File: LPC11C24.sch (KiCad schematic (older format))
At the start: 1 part

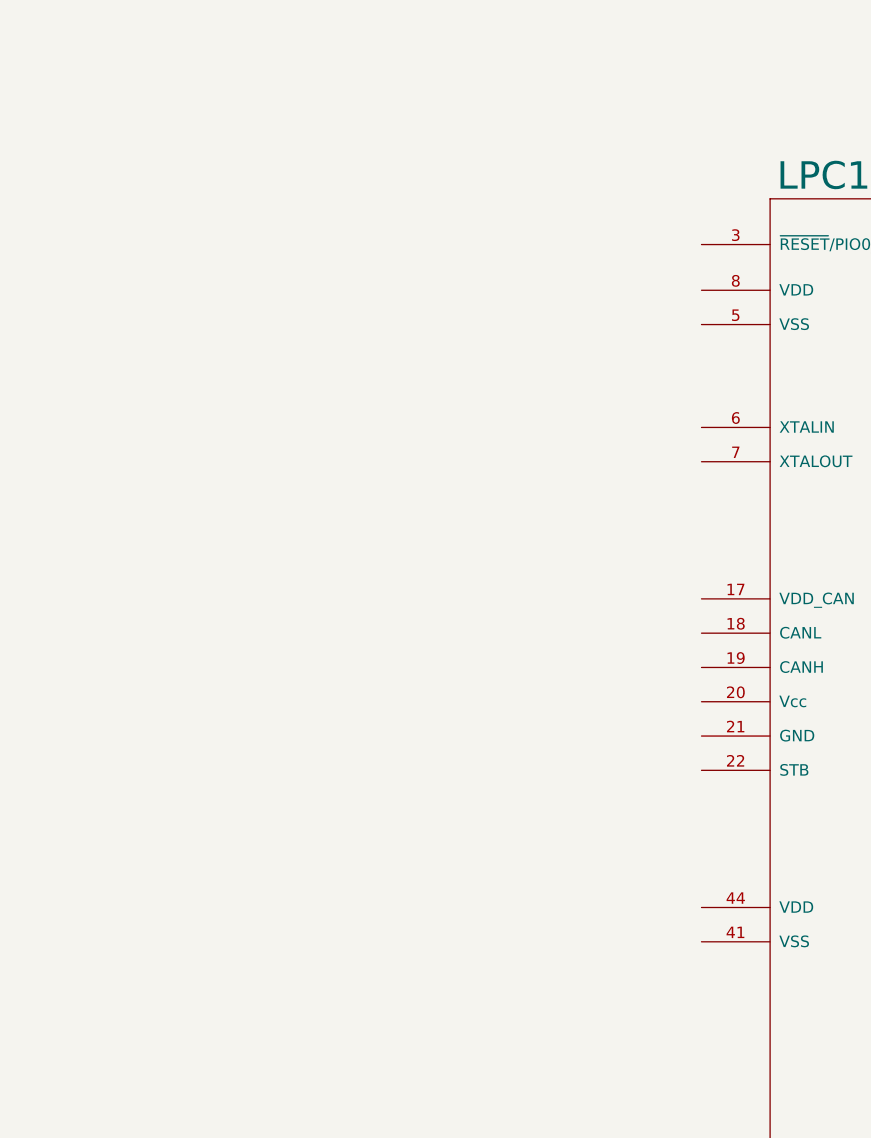
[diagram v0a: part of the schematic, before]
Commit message: Changed the controller symbol for the LPC11C24 added some of the support components,played with the larger blocks
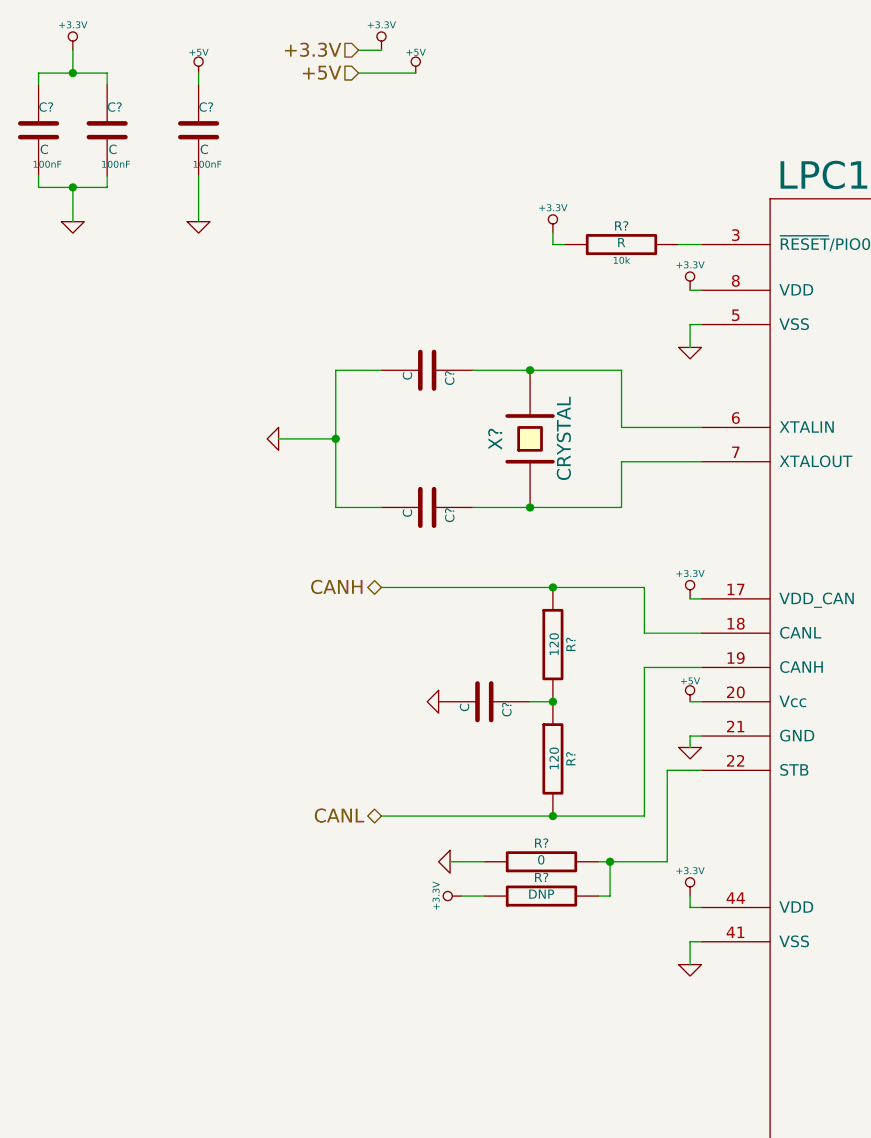
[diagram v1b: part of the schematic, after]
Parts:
- added C? (x3): C, ~, symbol C
- added C? (x3): C, 100nF, symbol C
- added R? (x2): 120, ~, symbol R
- added R?: R, 10k, symbol R
- added R?: 0, ~, symbol R
- added R?: DNP, ~, symbol R
- added X?: CRYSTAL, ~, symbol CRYSTAL
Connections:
- net +3.3V: now reaches U?.17 (VDD_CAN)
- net +3.3V: now also U?.44 (VDD), U?.8 (VDD), C?.1, C?.1, R?.1, R?.1
- net CANH: now reaches U?.18 (CANL)
- net CANH: now also R?.1
- net CANL: now reaches U?.19 (CANH)
- net CANL: now also R?.2
- net +5V: now reaches U?.20 (Vcc)
- net +5V: now also C?.1
- net GND: now reaches U?.21 (GND)
- net GND: now also U?.41 (VSS), U?.5 (VSS), C?.2, C?.2, C?.2, C?.2, C?.2, C?.2, R?.1
- net at U?.22 (STB): now also R?.2, R?.2
- net at U?.3 (~RESET~/PIO0_0): now also R?.2
- net at U?.6 (XTALIN): now also C?.1, X?.2
- net at U?.7 (XTALOUT): now also C?.1, X?.1
- new net: C?.1, R?.1, R?.2

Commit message: changed the voltage lbaels to global labels
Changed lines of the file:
@@
-EESchema Schematic File Version 2  date 4/14/2013 3:47:51 AM
+EESchema Schematic File Version 2  date 4/14/2013 1:14:12 PM
 LIBS:power
 LIBS:device
@@
 $Descr A4 11693 8268
 encoding utf-8
-Sheet 5 6
+Sheet 5 7
 Title ""
 Date "14 apr 2013"
@@
 Text HLabel 2400 4050 0    60   BiDi ~ 0
 CANL
-Text HLabel 2300 700  0    60   Input ~ 0
-+3.3V
-Text HLabel 2300 800  0    60   Input ~ 0
-+5V
-$Comp
-L +3.3V #PWR?
-U 1 1 516AB06C
-P 2400 700
-F 0 "#PWR?" H 2400 660 30  0001 C CNN
-F 1 "+3.3V" H 2400 810 30  0000 C CNN
-F 2 "" H 2400 700 60  0000 C CNN
-F 3 "" H 2400 700 60  0000 C CNN
-	1    2400 700
-	1    0    0    -1
-$EndComp
-$Comp
-L +5V #PWR?
-U 1 1 516AB072
-P 2550 800
-F 0 "#PWR?" H 2550 890 20  0001 C CNN
-F 1 "+5V" H 2550 890 30  0000 C CNN
-F 2 "" H 2550 800 60  0000 C CNN
-F 3 "" H 2550 800 60  0000 C CNN
-	1    2550 800
-	1    0    0    -1
-$EndComp
-Wire Wire Line
-	2300 800  2550 800
-Wire Wire Line
-	2400 700  2300 700
 $EndSCHEMATC

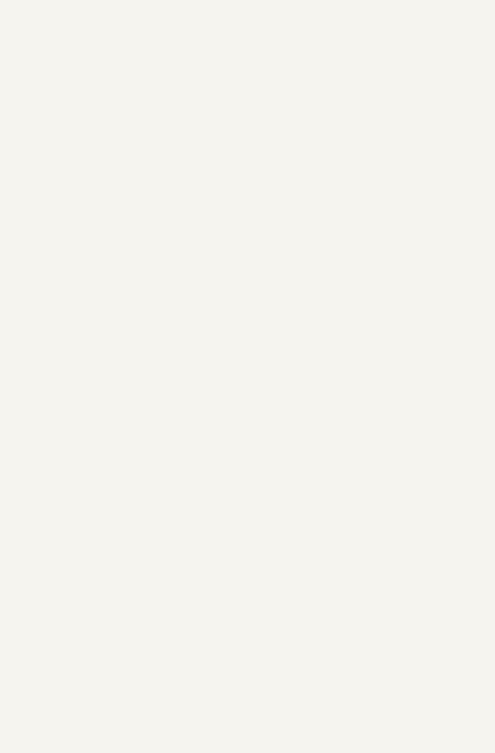
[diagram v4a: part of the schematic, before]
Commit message: added some stuff to the main controller schematic
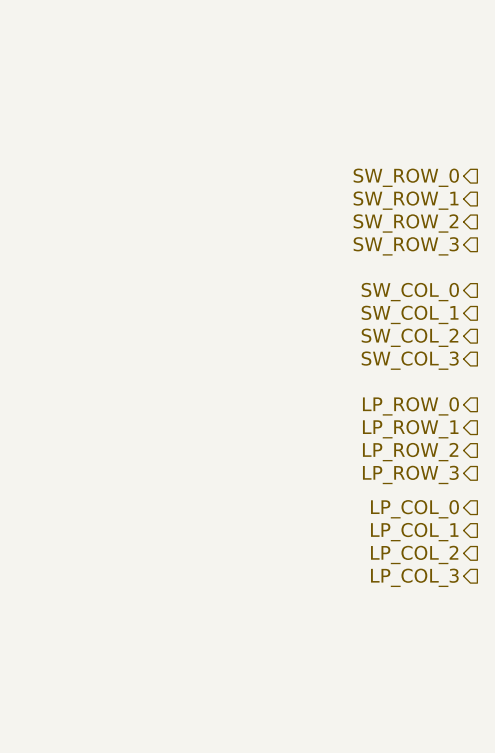
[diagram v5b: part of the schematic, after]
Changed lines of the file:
@@
-EESchema Schematic File Version 2  date 4/15/2013 12:46:04 AM
+EESchema Schematic File Version 2  date 4/15/2013 1:22:57 AM
 LIBS:power
 LIBS:device
@@
 Text HLabel 2400 4050 0    60   BiDi ~ 0
 CANL
+Text HLabel 10900 1600 0    60   Output ~ 0
+SW_ROW_0
+Text HLabel 10900 1700 0    60   Output ~ 0
+SW_ROW_1
+Text HLabel 10900 1800 0    60   Output ~ 0
+SW_ROW_2
+Text HLabel 10900 1900 0    60   Output ~ 0
+SW_ROW_3
+Text HLabel 10900 2100 0    60   Output ~ 0
+SW_COL_0
+Text HLabel 10900 2200 0    60   Output ~ 0
+SW_COL_1
+Text HLabel 10900 2300 0    60   Output ~ 0
+SW_COL_2
+Text HLabel 10900 2400 0    60   Output ~ 0
+SW_COL_3
+Text HLabel 10900 2600 0    60   Output ~ 0
+LP_ROW_0
+Text HLabel 10900 2700 0    60   Output ~ 0
+LP_ROW_1
+Text HLabel 10900 2800 0    60   Output ~ 0
+LP_ROW_2
+Text HLabel 10900 2900 0    60   Output ~ 0
+LP_ROW_3
+Text HLabel 10900 3050 0    60   Output ~ 0
+LP_COL_0
+Text HLabel 10900 3150 0    60   Output ~ 0
+LP_COL_1
+Text HLabel 10900 3250 0    60   Output ~ 0
+LP_COL_2
+Text HLabel 10900 3350 0    60   Output ~ 0
+LP_COL_3
 $EndSCHEMATC

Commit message: power updated still need to add underpad also changed input connector to 5 pin and added fuses, added current sense with op-amp for solinoids
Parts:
- added P?: CONN_4, symbol CONN_4
- added R? (x2): R, ~, symbol R
- R? (x2): value 120 -> 60
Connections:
- net labels added: ADC1, ADC2, ADC3, ADC4, ADC5, ADC6, ADC7, I2C_C, I2C_D
- wire segments 48 -> 66
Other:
- moved on the sheet: C?, R?, U?, X?

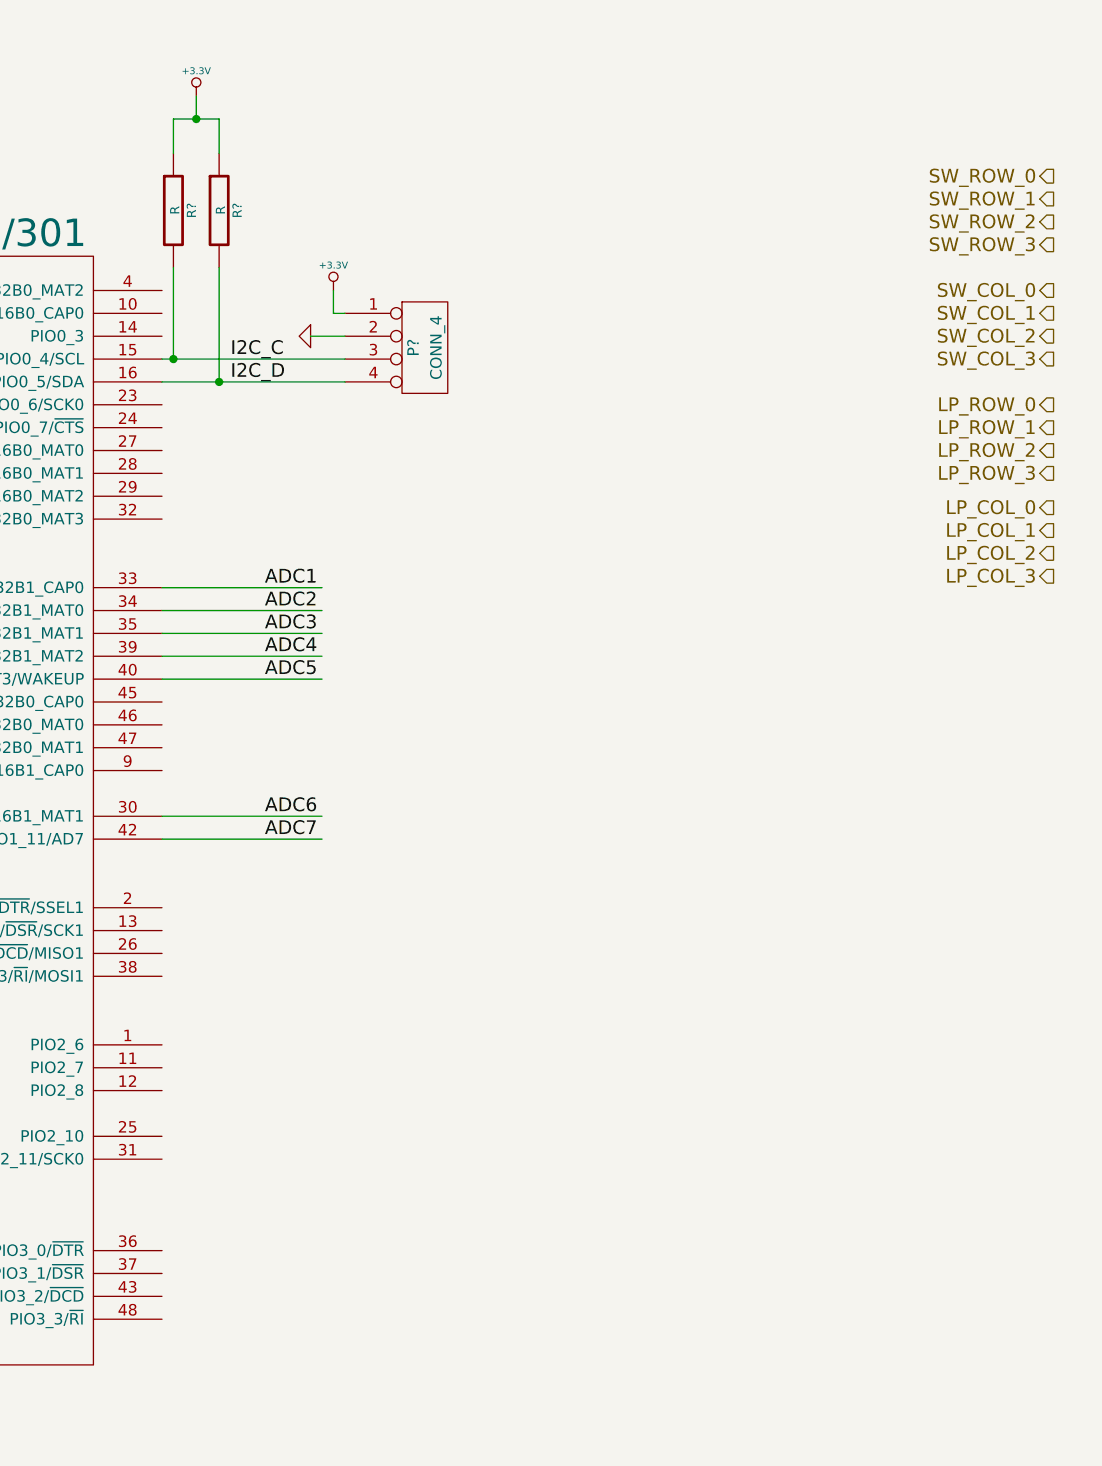
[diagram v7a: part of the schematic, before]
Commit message: added dip switch library and modifed current sense's to add capsstarted the main controller page
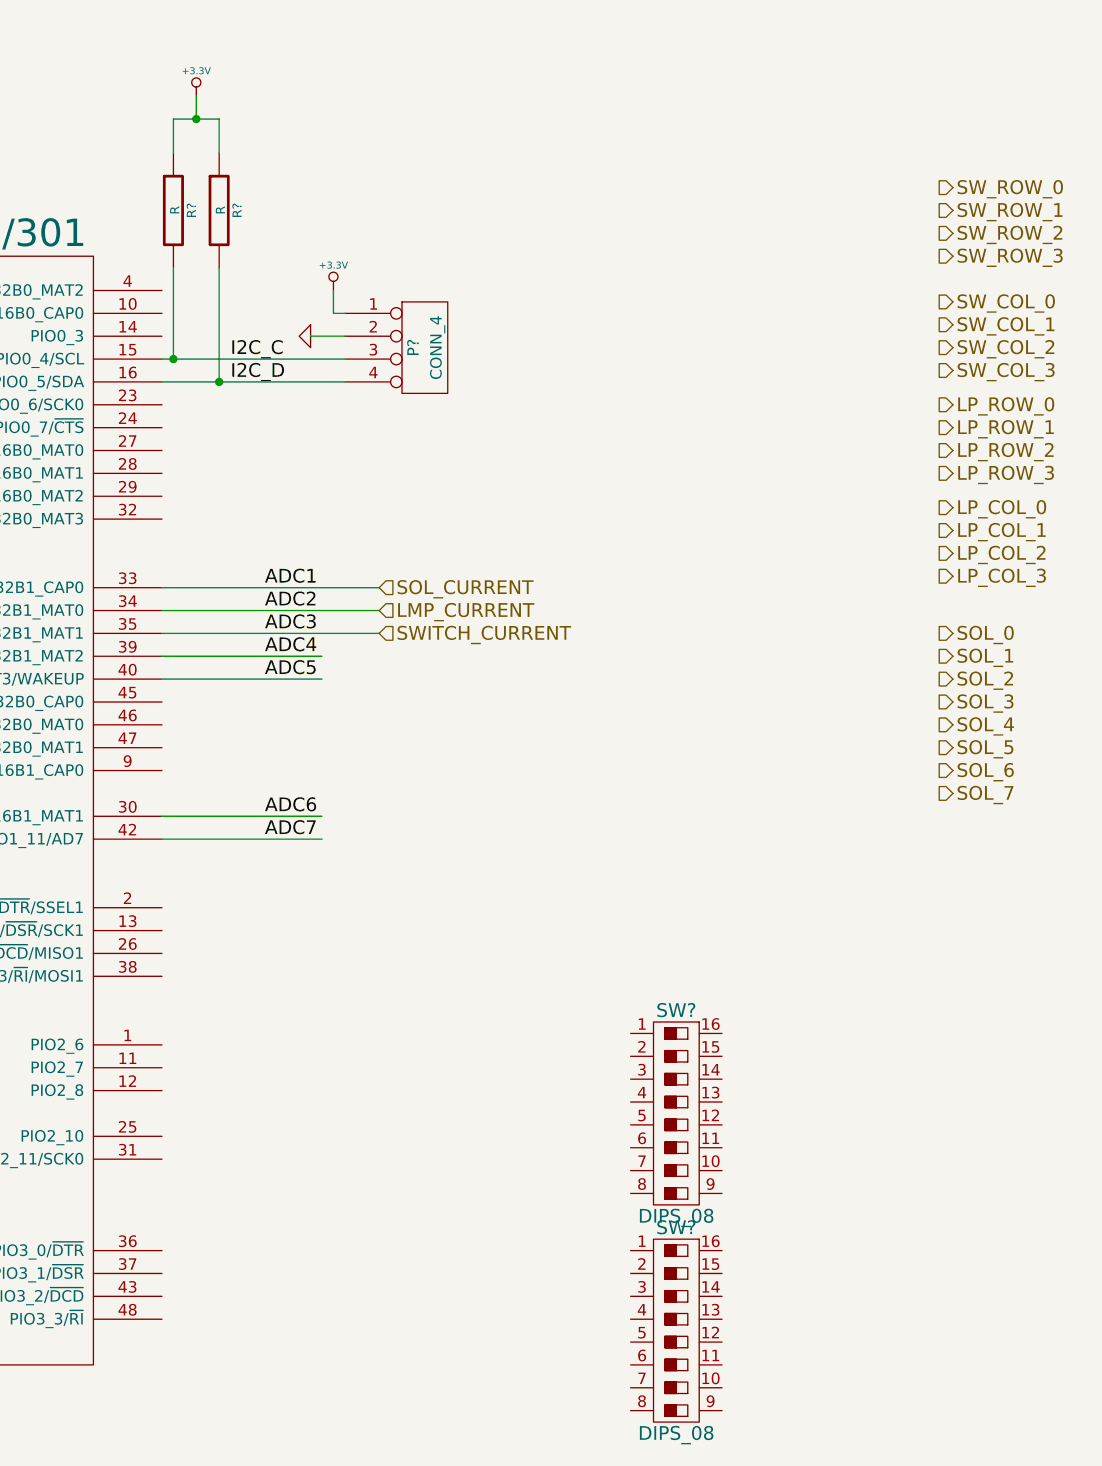
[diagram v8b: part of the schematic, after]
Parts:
- added SW? (x2): DIPS_08, symbol DIPS_08
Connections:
- net labels added: LMP_CURRENT, SOL_0, SOL_1, SOL_2, SOL_3, SOL_4, SOL_5, SOL_6, SOL_7, SOL_CURRENT, SWITCH_CURRENT
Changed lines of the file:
@@
-EESchema Schematic File Version 2  date 4/16/2013 2:34:18 AM
+EESchema Schematic File Version 2  date 4/16/2013 9:07:53 PM
 LIBS:power
 LIBS:device
@@
 LIBS:CurrentSense
 LIBS:pinball-power
+LIBS:dips-s
 LIBS:base-module-cache
 EELAYER 27 0
@@
 $Descr A4 11693 8268
 encoding utf-8
-Sheet 5 10
+Sheet 10 10
 Title ""
-Date "16 apr 2013"
+Date "17 apr 2013"
 Rev ""
 Comp ""
@@
 Text HLabel 1300 4650 0    60   BiDi ~ 0
 CANL
-Text HLabel 10900 1600 0    60   Output ~ 0
+Text HLabel 10400 1650 2    60   Output ~ 0
 SW_ROW_0
-Text HLabel 10900 1700 0    60   Output ~ 0
+Text HLabel 10400 1750 2    60   Output ~ 0
 SW_ROW_1
-Text HLabel 10900 1800 0    60   Output ~ 0
+Text HLabel 10400 1850 2    60   Output ~ 0
 SW_ROW_2
-Text HLabel 10900 1900 0    60   Output ~ 0
+Text HLabel 10400 1950 2    60   Output ~ 0
 SW_ROW_3
-Text HLabel 10900 2100 0    60   Output ~ 0
+Text HLabel 10400 2150 2    60   Output ~ 0
 SW_COL_0
-Text HLabel 10900 2200 0    60   Output ~ 0
+Text HLabel 10400 2250 2    60   Output ~ 0
 SW_COL_1
-Text HLabel 10900 2300 0    60   Output ~ 0
+Text HLabel 10400 2350 2    60   Output ~ 0
 SW_COL_2
-Text HLabel 10900 2400 0    60   Output ~ 0
+Text HLabel 10400 2450 2    60   Output ~ 0
 SW_COL_3
-Text HLabel 10900 2600 0    60   Output ~ 0
+Text HLabel 10400 2600 2    60   Output ~ 0
 LP_ROW_0
-Text HLabel 10900 2700 0    60   Output ~ 0
+Text HLabel 10400 2700 2    60   Output ~ 0
 LP_ROW_1
-Text HLabel 10900 2800 0    60   Output ~ 0
+Text HLabel 10400 2800 2    60   Output ~ 0
 LP_ROW_2
-Text HLabel 10900 2900 0    60   Output ~ 0
+Text HLabel 10400 2900 2    60   Output ~ 0
 LP_ROW_3
-Text HLabel 10900 3050 0    60   Output ~ 0
+Text HLabel 10400 3050 2    60   Output ~ 0
 LP_COL_0
-Text HLabel 10900 3150 0    60   Output ~ 0
+Text HLabel 10400 3150 2    60   Output ~ 0
 LP_COL_1
-Text HLabel 10900 3250 0    60   Output ~ 0
+Text HLabel 10400 3250 2    60   Output ~ 0
 LP_COL_2
-Text HLabel 10900 3350 0    60   Output ~ 0
+Text HLabel 10400 3350 2    60   Output ~ 0
 LP_COL_3
 Wire Wire Line
-	7000 3400 7700 3400
-Wire Wire Line
-	7700 3500 7000 3500
-Wire Wire Line
-	7000 3600 7700 3600
+	7000 3400 7950 3400
+Wire Wire Line
+	7000 3500 7950 3500
+Wire Wire Line
+	7000 3600 7950 3600
 Wire Wire Line
 	7700 3700 7000 3700
@@
 Wire Wire Line
 	7750 2200 7750 2100
+$Comp
+L DIPS_08 SW?
+U 1 1 516E9CFF
+P 9250 5700
+F 0 "SW?" V 8800 5700 60  0000 C CNN
+F 1 "DIPS_08" V 9700 5700 60  0000 C CNN
+F 2 "" H 9250 5700 60  0000 C CNN
+F 3 "" H 9250 5700 60  0000 C CNN
+	1    9250 5700
+	0    1    1    0
+$EndComp
+$Comp
+L DIPS_08 SW?
+U 1 1 516E9D16
+P 9250 6650
+F 0 "SW?" V 8800 6650 60  0000 C CNN
+F 1 "DIPS_08" V 9700 6650 60  0000 C CNN
+F 2 "" H 9250 6650 60  0000 C CNN
+F 3 "" H 9250 6650 60  0000 C CNN
+	1    9250 6650
+	0    1    1    0
+$EndComp
+Text HLabel 7950 3400 2    60   Input ~ 0
+SOL_CURRENT
+Text HLabel 7950 3500 2    60   Input ~ 0
+LMP_CURRENT
+Text HLabel 7950 3600 2    60   Input ~ 0
+SWITCH_CURRENT
+Text HLabel 10400 3600 2    60   Output ~ 0
+SOL_0
+Text HLabel 10400 3700 2    60   Output ~ 0
+SOL_1
+Text HLabel 10400 3800 2    60   Output ~ 0
+SOL_2
+Text HLabel 10400 3900 2    60   Output ~ 0
+SOL_3
+Text HLabel 10400 4000 2    60   Output ~ 0
+SOL_4
+Text HLabel 10400 4100 2    60   Output ~ 0
+SOL_5
+Text HLabel 10400 4200 2    60   Output ~ 0
+SOL_6
+Text HLabel 10400 4300 2    60   Output ~ 0
+SOL_7
 $EndSCHEMATC
